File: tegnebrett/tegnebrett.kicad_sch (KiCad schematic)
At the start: 45 parts, among them J1 FH12-45S-0.5SH55, J2 FH12-6S-1SH55, J3 Conn_ST_STDC14, J4 USB-A1HSW6, J5 MCU_Header_Pin, SW1 SW_Push, SW2 SW_Push, SW3 MCU_Button, SW4 Reset, SW5 Undo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

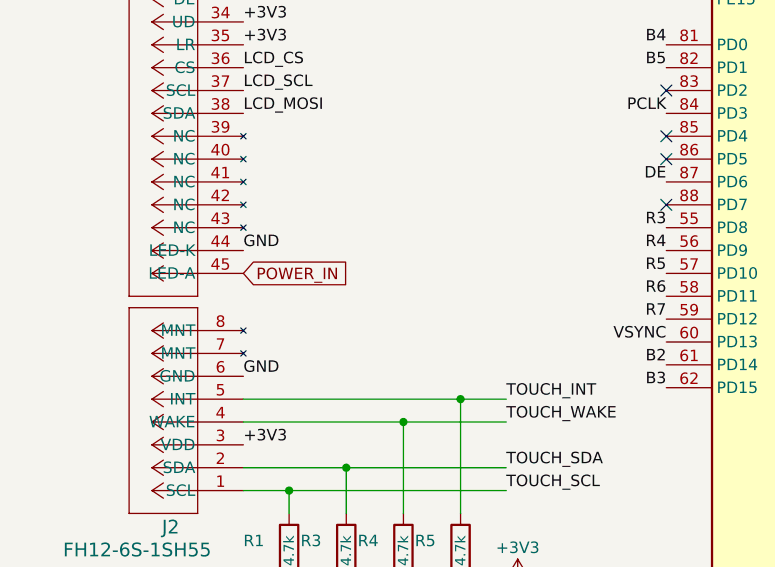
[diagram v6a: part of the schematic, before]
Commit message: fix: add resistor to LCD screen
To ensure that we don't get a situation where the current through the
LCD blows up.
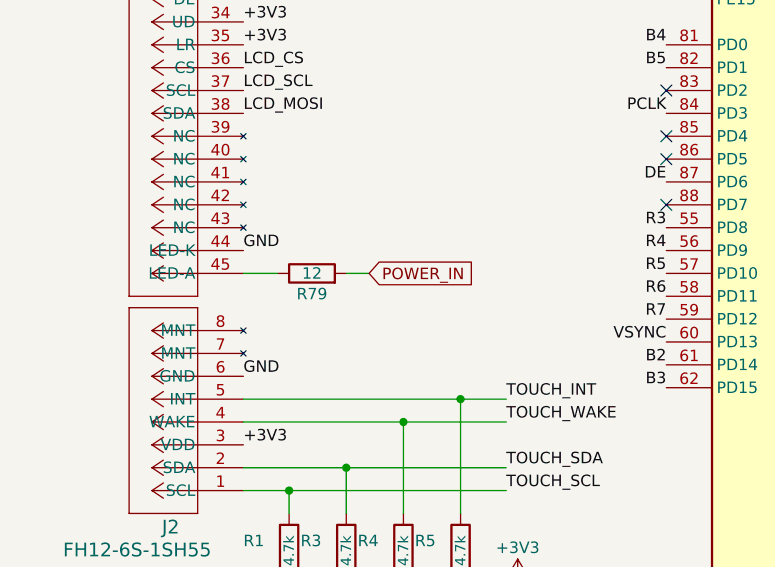
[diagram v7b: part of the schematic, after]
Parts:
- added R79: 12, Resistor_SMD:R_0805_2012Metric_Pad1.20x1.40mm_HandSolder, symbol Device:R
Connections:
- net POWER_IN: now also R79.2; no longer J1.45 (LED-A)
- new net: J1.45 (LED-A), R79.1
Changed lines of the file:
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@@
 	(wire
 		(pts
+			(xy 36.83 142.24) (xy 40.64 142.24)
+		)
+		(stroke
+			(width 0)
+			(type default)
+		)
+	)
+	(wire
+		(pts
 			(xy 46.99 88.9) (xy 53.34 88.9)
 		)
@@
 	(wire
 		(pts
+			(xy 48.26 142.24) (xy 50.8 142.24)
+		)
+		(stroke
+			(width 0)
+			(type default)
+		)
+	)
+	(wire
+		(pts
 			(xy 36.83 38.1) (xy 48.26 38.1)
 		)
@@
 	(global_label "POWER_IN"
 		(shape input)
-		(at 36.83 142.24 0)
+		(at 50.8 142.24 0)
 		(fields_autoplaced yes)
 		(effects
@@
 		)
 		(property "Intersheetrefs" "${INTERSHEET_REFS}"
-			(at 49.189 142.24 0)
+			(at 63.159 142.24 0)
 			(effects
 				(font
@@
 					(unit 1)
 				)
+			)
+		)
+	)
+	(symbol
+		(lib_id "Device:R")
+		(at 44.45 142.24 90)
+		(unit 1)
+		(exclude_from_sim no)
+		(in_bom yes)
+		(on_board yes)
+		(dnp no)
+		(property "Reference" "R79"
+			(at 44.45 144.526 90)
+			(effects
+				(font
+					(size 1.27 1.27)
+				)
+			)
+		)
+		(property "Value" "12"
+			(at 44.45 142.24 90)
+			(effects
+				(font
+					(size 1.27 1.27)
+				)
+			)
+		)
+		(property "Footprint" "Resistor_SMD:R_0805_2012Metric_Pad1.20x1.40mm_HandSolder"
+			(at 44.45 144.018 90)
+			(effects
+				(font
+					(size 1.27 1.27)
+				)
+				(hide yes)
+			)
+		)
+		(property "Datasheet" "~"
+			(at 44.45 142.24 0)
+			(effects
+				(font
+					(size 1.27 1.27)
+				)
+				(hide yes)
+			)
+		)
+		(property "Description" "Resistor"
+			(at 44.45 142.24 0)
+			(effects
+				(font
+					(size 1.27 1.27)
+				)
+				(hide yes)
+			)
+		)
+		(pin "2"
+		)
+		(pin "1"
+		)
+		(instances
+			(project ""
+				(path "/d9a31669-c5f1-42a7-9461-3df04b9a4e62"
+					(reference "R79")
+					(unit 1)
+				)

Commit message: fix: add power flag to remove error
This is for the power going into the LCD backlight.
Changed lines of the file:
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@@
 	)
 	(junction
+		(at 39.37 142.24)
+		(diameter 0)
+		(color 0 0 0 0)
+	)
+	(junction
 		(at 48.26 38.1)
 		(diameter 0)
@@
 	(wire
 		(pts
-			(xy 36.83 142.24) (xy 40.64 142.24)
+			(xy 36.83 142.24) (xy 39.37 142.24)
 		)
 		(stroke
@@
 	(wire
 		(pts
-			(xy 48.26 142.24) (xy 50.8 142.24)
+			(xy 48.26 142.24) (xy 53.34 142.24)
 		)
 		(stroke
@@
 	(wire
 		(pts
+			(xy 39.37 142.24) (xy 40.64 142.24)
+		)
+		(stroke
+			(width 0)
+			(type default)
+		)
+	)
+	(wire
+		(pts
 			(xy 196.85 27.94) (xy 196.85 30.48)
 		)
@@
 	(global_label "POWER_IN"
 		(shape input)
-		(at 50.8 142.24 0)
+		(at 53.34 142.24 0)
 		(fields_autoplaced yes)
 		(effects
@@
 		)
 		(property "Intersheetrefs" "${INTERSHEET_REFS}"
-			(at 63.159 142.24 0)
+			(at 65.699 142.24 0)
 			(effects
 				(font
@@
 	)
 	(symbol
+		(lib_id "power:PWR_FLAG")
+		(at 39.37 142.24 180)
+		(unit 1)
+		(exclude_from_sim no)
+		(in_bom yes)
+		(on_board yes)
+		(dnp no)
+		(property "Reference" "#FLG09"
+			(at 39.37 144.145 0)
+			(effects
+				(font
+					(size 1.27 1.27)
+				)
+				(hide yes)
+			)
+		)
+		(property "Value" "PWR_FLAG"
+			(at 39.37 145.796 0)
+			(effects
+				(font
+					(size 1.27 1.27)
+				)
+			)
+		)
+		(property "Footprint" ""
+			(at 39.37 142.24 0)
+			(effects
+				(font
+					(size 1.27 1.27)
+				)
+				(hide yes)
+			)
+		)
+		(property "Datasheet" "~"
+			(at 39.37 142.24 0)
+			(effects
+				(font
+					(size 1.27 1.27)
+				)
+				(hide yes)
+			)
+		)
+		(property "Description" "Special symbol for telling ERC where power comes from"
+			(at 39.37 142.24 0)
+			(effects
+				(font
+					(size 1.27 1.27)
+				)
+				(hide yes)
+			)
+		)
+		(pin "1"
+		)
+		(instances
+			(project ""
+				(path "/d9a31669-c5f1-42a7-9461-3df04b9a4e62"
+					(reference "#FLG09")
+					(unit 1)
+				)
+			)
+		)
+	)
+	(symbol
 		(lib_id "Switch:SW_Push")
 		(at 76.2 44.45 90)
@@
 		(dnp no)
 		(property "Reference" "R79"
-			(at 44.45 144.526 90)
+			(at 44.45 139.954 90)
 			(effects
 				(font
